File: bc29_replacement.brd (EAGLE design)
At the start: 120.7 x 86.4 mm, 42 parts, among them IC1 74HCS596D, IC17 CD4070B, IC18 LP2951, J2 2520-, M1 IRF740, U9 MSP430I2041TPW, X1 236-412

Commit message: power
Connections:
- net +BATT: no longer F1.1
- net +BATT_FILT: now also F1.1
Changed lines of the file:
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@@
 </signal>
 <signal name="+BATT">
-<contactref element="F1" pad="1"/>
 <contactref element="X1" pad="1@1"/>
 <contactref element="L1" pad="1"/>
-<wire x1="3.81" y1="71.12" x2="41.91" y2="80.01" width="0" layer="19" extent="1-1"/>
 <wire x1="21.94" y1="52.81" x2="3.81" y2="71.12" width="0" layer="19" extent="1-1"/>
 </signal>
@@
 <contactref element="L1" pad="2"/>
 <contactref element="C2" pad="+"/>
+<contactref element="F1" pad="1"/>
+<wire x1="29.21" y1="67.31" x2="41.91" y2="80.01" width="0" layer="19" extent="1-1"/>
 <wire x1="33.94" y1="56.41" x2="29.21" y2="67.31" width="0" layer="19" extent="1-1"/>
 </signal>

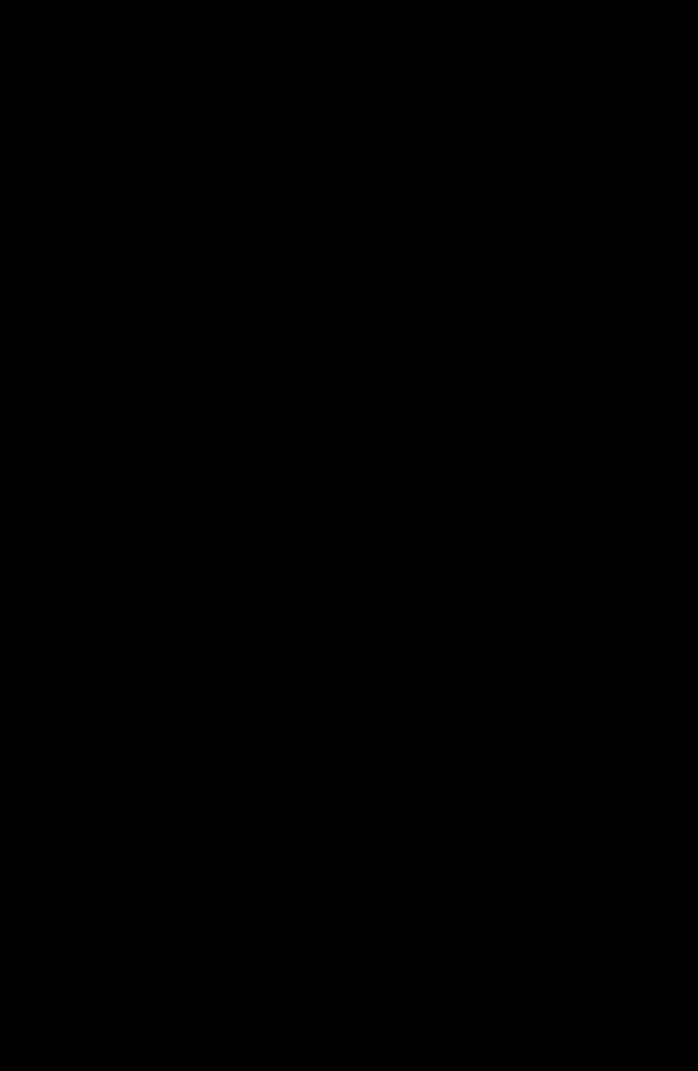
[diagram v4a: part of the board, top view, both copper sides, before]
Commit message: add shift register
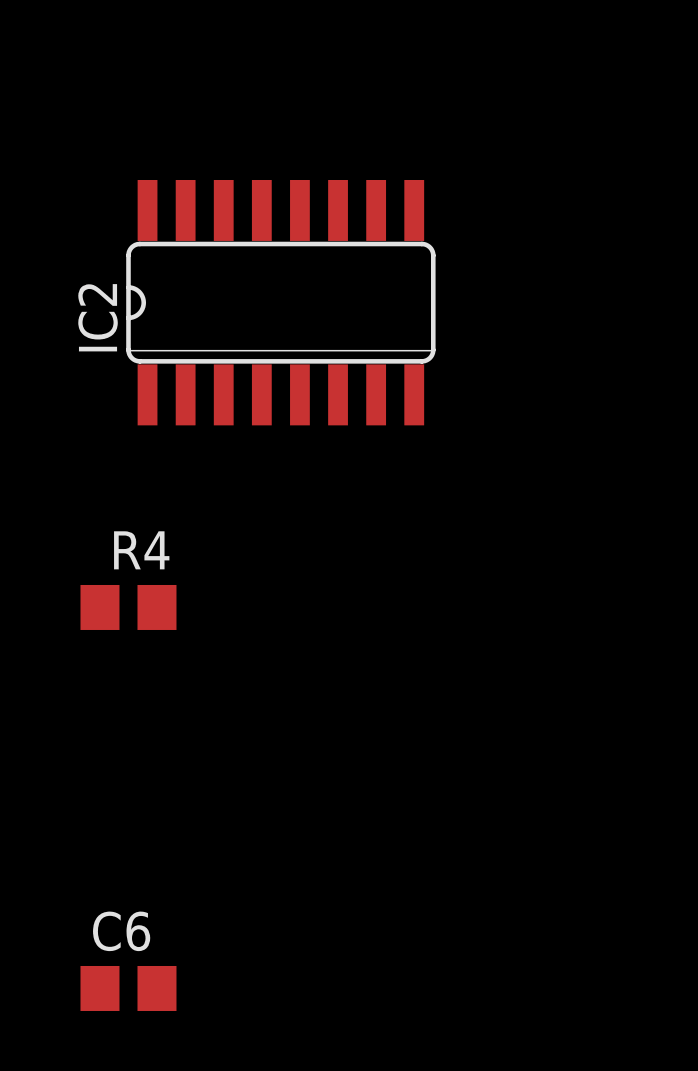
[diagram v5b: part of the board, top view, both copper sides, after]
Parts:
- added C6: .1uF, rcl:C0805
- added IC2: 74HCS596D, 74xx-us:SO16
- added R4: 20.0K, rcl:R0805
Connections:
- new net N$4: IC1.9, IC2.14
- new net RCK: IC1.12, IC2.12
- new net SCK: IC1.11, IC2.11
- new net SCL: IC1.10, IC2.10, R4.1
- net GND: now also IC1.13, IC2.13, IC2.8
- net VCC: now also IC2.16, R4.2
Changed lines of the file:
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@@
 <element name="C5" library="rcl" package="C0805" value="47pF" x="107.95" y="8.89"/>
 <element name="IC1" library="74xx-us" package="SO16" value="74HCS596D" x="97.79" y="55.88"/>
+<element name="IC2" library="74xx-us" package="SO16" value="74HCS596D" x="-12.7" y="0"/>
+<element name="C6" library="rcl" package="C0805" value=".1uF" x="-17.78" y="-22.86"/>
+<element name="R4" library="rcl" package="R0805" value="20.0K " x="-17.78" y="-10.16"/>
 </elements>
 <signals>
@@
 <contactref element="C4" pad="2"/>
 <contactref element="IC1" pad="8"/>
-<wire x1="77.47" y1="72.39" x2="98.1711" y2="75.832" width="0" layer="19" extent="1-1"/>
-<wire x1="73.66" y1="68.58" x2="77.47" y2="72.39" width="0" layer="19" extent="1-1"/>
-<wire x1="73.79" y1="55.88" x2="73.66" y2="68.58" width="0" layer="19" extent="1-1"/>
-<wire x1="80.96" y1="55.88" x2="73.79" y2="55.88" width="0" layer="19" extent="1-1"/>
-<wire x1="66.675" y1="50.74" x2="73.79" y2="55.88" width="0" layer="19" extent="1-1"/>
-<wire x1="84.25" y1="38.1" x2="80.96" y2="55.88" width="0" layer="19" extent="1-1"/>
+<contactref element="IC2" pad="8"/>
+<contactref element="IC1" pad="13"/>
+<contactref element="IC2" pad="13"/>
+<wire x1="97.155" y1="58.9534" x2="98.1711" y2="75.832" width="0" layer="19" extent="1-1"/>
+<wire x1="102.235" y1="52.8066" x2="97.155" y2="58.9534" width="0" layer="19" extent="1-1"/>
+<wire x1="104.46" y1="40.64" x2="102.235" y2="52.8066" width="0" layer="19" extent="1-1"/>
+<wire x1="112.08" y1="40.64" x2="104.46" y2="40.64" width="0" layer="19" extent="1-1"/>
+<wire x1="96.84" y1="40.64" x2="104.46" y2="40.64" width="0" layer="19" extent="1-1"/>
+<wire x1="84.25" y1="38.1" x2="96.84" y2="40.64" width="0" layer="19" extent="1-1"/>
 <wire x1="86.04" y1="30.48" x2="84.25" y2="38.1" width="0" layer="19" extent="1-1"/>
 <wire x1="81.8388" y1="25.1206" x2="86.04" y2="30.48" width="0" layer="19" extent="1-1"/>
-<wire x1="96.84" y1="40.64" x2="84.25" y2="38.1" width="0" layer="19" extent="1-1"/>
-<wire x1="104.46" y1="40.64" x2="96.84" y2="40.64" width="0" layer="19" extent="1-1"/>
-<wire x1="112.08" y1="40.64" x2="104.46" y2="40.64" width="0" layer="19" extent="1-1"/>
 <wire x1="107" y1="27.94" x2="104.46" y2="40.64" width="0" layer="19" extent="1-1"/>
 <wire x1="108.9" y1="15.24" x2="107" y2="27.94" width="0" layer="19" extent="1-1"/>
 <wire x1="68.9" y1="30.48" x2="81.8388" y2="25.1206" width="0" layer="19" extent="1-1"/>
 <wire x1="58.42" y1="21.0566" x2="68.9" y2="30.48" width="0" layer="19" extent="1-1"/>
+<wire x1="80.96" y1="55.88" x2="97.155" y2="58.9534" width="0" layer="19" extent="1-1"/>
+<wire x1="73.79" y1="55.88" x2="80.96" y2="55.88" width="0" layer="19" extent="1-1"/>
+<wire x1="66.675" y1="50.74" x2="73.79" y2="55.88" width="0" layer="19" extent="1-1"/>
+<wire x1="73.66" y1="68.58" x2="73.79" y2="55.88" width="0" layer="19" extent="1-1"/>
+<wire x1="77.47" y1="72.39" x2="73.66" y2="68.58" width="0" layer="19" extent="1-1"/>
 <wire x1="50.8" y1="68.58" x2="73.66" y2="68.58" width="0" layer="19" extent="1-1"/>
 <wire x1="36.83" y1="67.31" x2="50.8" y2="68.58" width="0" layer="19" extent="1-1"/>
@@
 <wire x1="33.02" y1="22.86" x2="42.86" y2="38.1" width="0" layer="19" extent="1-1"/>
 <wire x1="3.81" y1="66.04" x2="36.83" y2="67.31" width="0" layer="19" extent="1-1"/>
-<wire x1="102.235" y1="52.8066" x2="33.02" y2="22.86" width="0" layer="19" extent="1-1"/>
+<wire x1="-8.255" y1="-3.0734" x2="33.02" y2="22.86" width="0" layer="19" extent="1-1"/>
+<wire x1="-13.335" y1="3.0734" x2="-8.255" y2="-3.0734" width="0" layer="19" extent="1-1"/>
 </signal>
 <signal name="+5V">
@@
 <contactref element="D1" pad="3"/>
 <contactref element="IC1" pad="16"/>
-<wire x1="113.98" y1="40.64" x2="98.8211" y2="75.832" width="0" layer="19" extent="1-1"/>
-<wire x1="84.14" y1="30.48" x2="113.98" y2="40.64" width="0" layer="19" extent="1-1"/>
+<contactref element="IC2" pad="16"/>
+<contactref element="R4" pad="2"/>
+<wire x1="93.345" y1="58.9534" x2="98.8211" y2="75.832" width="0" layer="19" extent="1-1"/>
+<wire x1="113.98" y1="40.64" x2="93.345" y2="58.9534" width="0" layer="19" extent="1-1"/>
+<wire x1="84.14" y1="30.48" x2="93.345" y2="58.9534" width="0" layer="19" extent="1-1"/>
 <wire x1="63.18" y1="30.48" x2="84.14" y2="30.48" width="0" layer="19" extent="1-1"/>
 <wire x1="62.23" y1="39.2" x2="63.18" y2="30.48" width="0" layer="19" extent="1-1"/>
-<wire x1="93.345" y1="58.9534" x2="63.18" y2="30.48" width="0" layer="19" extent="1-1"/>
+<wire x1="-17.145" y1="3.0734" x2="63.18" y2="30.48" width="0" layer="19" extent="1-1"/>
+<wire x1="-16.83" y1="-10.16" x2="-17.145" y2="3.0734" width="0" layer="19" extent="1-1"/>
 </signal>
 <signal name="UCA0TXD">
@@
 <contactref element="U9" pad="10"/>
 <contactref element="R10" pad="2"/>
-<wire x1="70.8" y1="40.64" x2="70.8" y2="30.48" width="0" layer="19" extent="1-1"/>
+<wire x1="70.8" y1="40.64" x2="96.8711" y2="75.832" width="0" layer="19" extent="1-1"/>
+<wire x1="70.8" y1="30.48" x2="70.8" y2="40.64" width="0" layer="19" extent="1-1"/>
 <wire x1="96.15" y1="30.48" x2="70.8" y2="30.48" width="0" layer="19" extent="1-1"/>
-<wire x1="96.8711" y1="75.832" x2="70.8" y2="40.64" width="0" layer="19" extent="1-1"/>
 </signal>
 <signal name="A0.0+">
@@
 <wire x1="99.25" y1="7.62" x2="108.9" y2="21.59" width="0" layer="19" extent="1-1"/>
 </signal>
+<signal name="N$4">
+<contactref element="IC1" pad="9"/>
+<contactref element="IC2" pad="14"/>
+<wire x1="-14.605" y1="3.0734" x2="102.235" y2="58.9534" width="0" layer="19" extent="1-1"/>
+</signal>
+<signal name="SCK">
+<contactref element="IC1" pad="11"/>
+<contactref element="IC2" pad="11"/>
+<wire x1="-10.795" y1="3.0734" x2="99.695" y2="58.9534" width="0" layer="19" extent="1-1"/>
+</signal>
+<signal name="SCL">
+<contactref element="IC2" pad="10"/>
+<contactref element="R4" pad="1"/>
+<contactref element="IC1" pad="10"/>
+<wire x1="-9.525" y1="3.0734" x2="100.965" y2="58.9534" width="0" layer="19" extent="1-1"/>
+<wire x1="-18.73" y1="-10.16" x2="-9.525" y2="3.0734" width="0" layer="19" extent="1-1"/>
+</signal>
+<signal name="RCK">
+<contactref element="IC1" pad="12"/>
+<contactref element="IC2" pad="12"/>
+<wire x1="-12.065" y1="3.0734" x2="98.425" y2="58.9534" width="0" layer="19" extent="1-1"/>
+</signal>
 </signals>
